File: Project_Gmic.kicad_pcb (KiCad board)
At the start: 2 copper layers, 55.9 x 62.2 mm, 50 parts, among them J1 USB4085-GF-A, J2 SJ1-3523N, SW1 SW_SPDT, U1 MCP6479, U2 MCP6476U, U3 MCP6476U, U4 XC6351A120MR-G

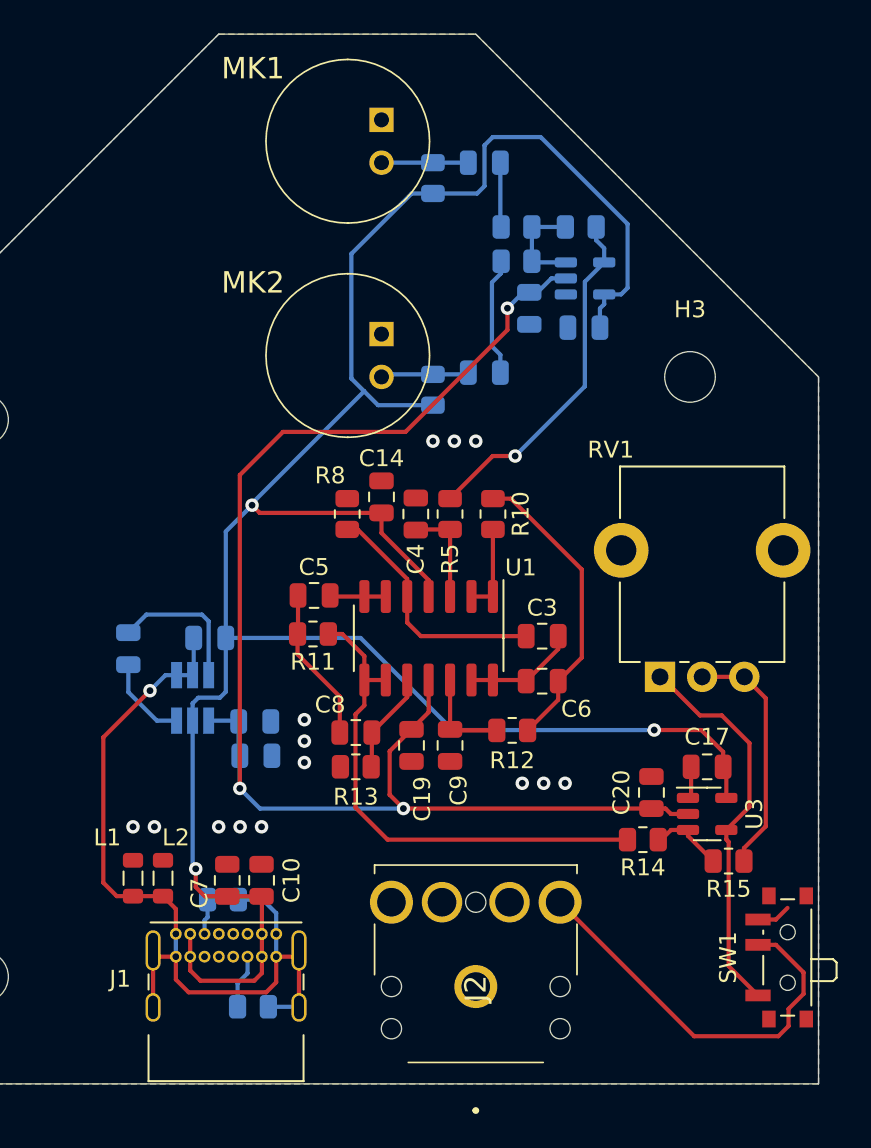
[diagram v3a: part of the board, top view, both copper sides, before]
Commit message: BOM, finishing PCB, changing some non-available components
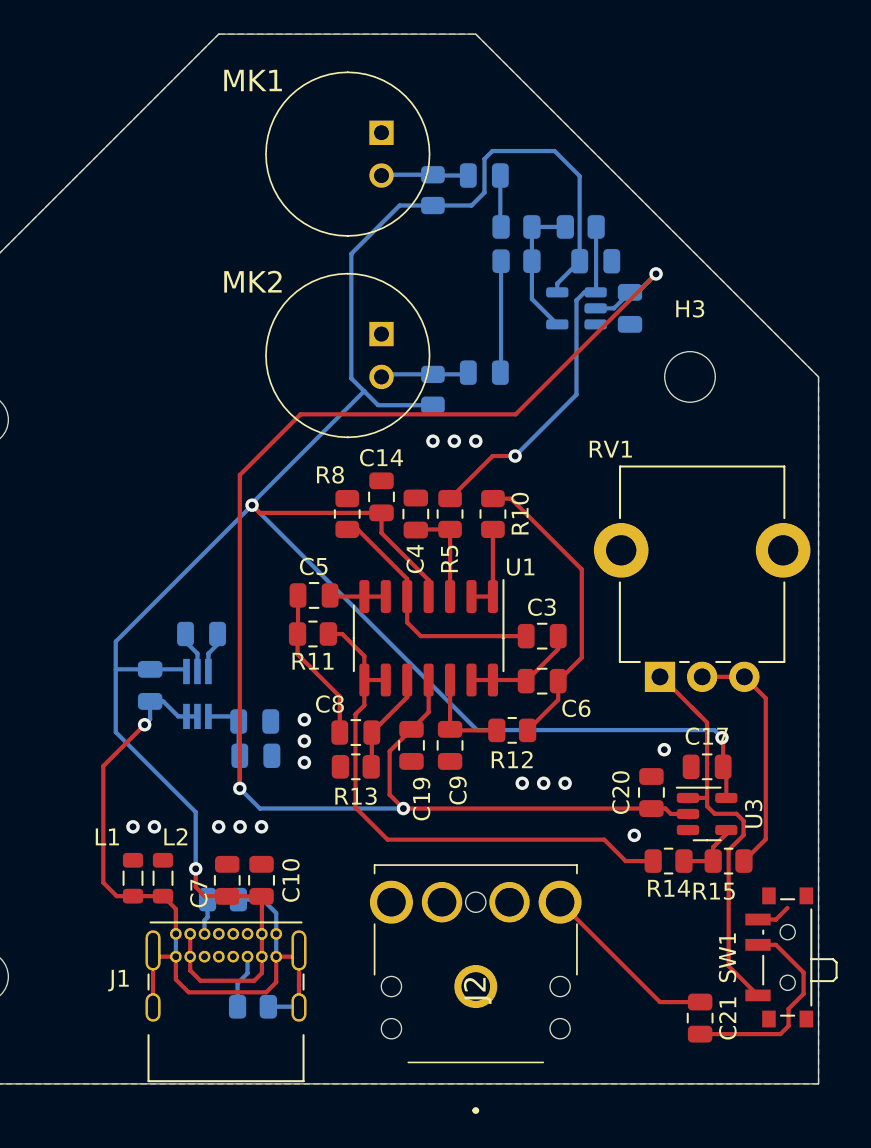
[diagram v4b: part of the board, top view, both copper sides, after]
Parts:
- added C21: NC, Capacitor_SMD:C_0805_2012Metric, F.Cu at (97.1, 149.8)
- R1, R2: value 2k2 -> 2.2k
- SW1: value SW_SPDT -> PCM12SMTR
- U2, U3: value MCP6476U -> AD8531
- U4: value XC6351A120MR-G -> MAX1852; footprint Package_TO_SOT_SMD:SOT-23-6_Handsoldering -> Package_TO_SOT_SMD:SOT-363_SC-70-6_Handsoldering
- moved C18 5.97 mm to (93.0, 107.7)
- moved C16 4.52 mm to (64.5, 130.0), turned to 270 degrees
- moved C15 4.43 mm to (67.6, 127.0), turned to 180 degrees
- moved C13 4.00 mm to (90.9, 104.9), turned to 0 degrees
- moved R14 1.98 mm to (95.2, 140.5)
- moved U2 1.85 mm to (89.8, 107.7), turned to 180 degrees
- moved C1 0.76 mm to (84.3, 99.8)
- moved MK1 0.76 mm to (78.2, 97.3)
- moved R1 0.72 mm to (81.3, 100.7)
- moved U4 0.37 mm to (67.3, 130.6), turned to 90 degrees
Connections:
- J2 pad 2: Net-(J2-Pad2) -> Net-(C21-Pad1)
- SW1 pad 2: Net-(J2-Pad2) -> Net-(C21-Pad2)
- U2 pad 1: GNDA -> /AUDIO_AVERAGE
- U2 pad 3: Net-(R6-Pad1) -> GNDA
- U2 pad 4: /AUDIO_AVERAGE -> Net-(R6-Pad1)
- U3 pad 1: GNDA -> /AUDIO_OUT
- U3 pad 3: Net-(R14-Pad1) -> GNDA
- U3 pad 4: /AUDIO_OUT -> Net-(R14-Pad1)
- U4 pad 1: GND -> -5V
- U4 pad 3: Net-(C15-Pad1) -> GND
- U4 pad 4: -5V -> +5V
- U4 pad 5: +5V -> Net-(C15-Pad2)
- U4 pad 6: Net-(C15-Pad2) -> Net-(C15-Pad1)
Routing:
- net Net-(J2-Pad2): track 24.0 -> 0.00 mm
- net Net-(C21-Pad2): track 0.00 -> 12.4 mm
- net Net-(C21-Pad1): track 0.00 -> 11.5 mm
- net -5V: track 85.4 -> 95.0 mm
- net Net-(C15-Pad1): track 8.56 -> 2.45 mm
- net +5V: track 142.1 -> 146.9 mm
- net Net-(C15-Pad2): track 5.19 -> 2.52 mm
- net GND: track 51.6 -> 49.0 mm
- net Net-(R6-Pad1): track 6.06 -> 8.48 mm
- net /AUDIO_PASS_HIGH: track 30.1 -> 32.1 mm
- net GNDA: track 3.96 -> 2.04 mm, vias 14 -> 16
- net /AUDIO_OUT: track 23.2 -> 24.7 mm
- net /AUDIO_1_IN: track 3.83 -> 3.07 mm
- net /AUDIO_AVERAGE: track 20.9 -> 21.5 mm
- net Net-(R14-Pad1): track 4.46 -> 3.90 mm

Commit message: Finalizing PCB, gerbert file
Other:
- rule pad_to_mask_clearance: 0.051 -> 0
- board text added: "GG"
- board text added: "GMIC V1.0"
- board text added: "Licensed under CERN-OHL-W v2 or later"

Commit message: moving to kicad 7, redo simulations WIP
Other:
- net class Default removed

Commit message: updating schematic, updating BOM
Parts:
- removed L1, L2: BLM21PG331SN1D, Inductor_SMD:L_0805_2012Metric
- added C22: 1uF, Capacitor_SMD:C_0805_2012Metric, F.Cu at (127.8, 130.5)
- added C23: 1uF, Capacitor_SMD:C_0805_2012Metric, F.Cu at (127.8, 133.5)
- added C24: 100nF, Capacitor_SMD:C_0805_2012Metric, F.Cu at (127.8, 136.5)
- added R16: 10k, Resistor_SMD:R_0805_2012Metric, F.Cu at (132.2, 134.9)
- added U5: TC1055, Package_TO_SOT_SMD:SOT-23-5, F.Cu at (132.6, 131.2)
- C10, C16: value 1uF -> 100nF
- C11, C17, C19: value 100nF -> 1uF
- C12: value 1uF -> 2.2uF
- C13, C20: value 100nF -> 2.2uF
- C21: value NC -> 100nF
- C8: value 100nF -> 100pF
- C9: value 100pF -> 1uF
- R10, R11, R8: value 80k -> 100k
- R14: value 100k -> 50k
- R15: value 80k -> 10k
- R2: value 2.2k -> 5.1k
- R3: value 5.1k -> 2.2k
- R6, R7: value 2.2k -> 80k
- RV1: value PTV09A-5025F-A503 -> PTV09A-4020F-A504; footprint Potentiometer_THT:Potentiometer_Alpha_RD901F-40-00D_Single_Vertical_CircularHoles -> PTV09A-4:PTV09A-4
- U1: value MCP6479 -> AD8532; footprint Package_SO:SOIC-14_3.9x8.7mm_P1.27mm -> Package_SO:SOIC-8_3.9x4.9mm_P1.27mm
- U2, U3: value AD8531 -> AD8532; footprint Package_TO_SOT_SMD:SOT-23-5 -> Package_SO:SOIC-8_3.9x4.9mm_P1.27mm
- U4: value MAX1852 -> AD8531; footprint Package_TO_SOT_SMD:SOT-363_SC-70-6_Handsoldering -> Package_TO_SOT_SMD:SOT-23-5
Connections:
- C10 pad 1: +5V -> +3.3V
- C11 pad 1: GNDA -> +3.3V
- C11 pad 2: -5V -> GNDA
- C12 pad 1: GNDA -> /AUDIO_OUT
- C12 pad 2: -5V -> /AUDIO_PASS_HIGH
- C13 pad 1: +5V -> Net-(U4-+)
- C14 pad 1: +5V -> +3.3V
- C15 pad 1: Net-(C15-Pad1) -> +3.3V
- C15 pad 2: Net-(C15-Pad2) -> GNDA
- C16 pad 1: +5V -> +3.3V
- C16 pad 2: GND -> GNDA
- C17 pad 1: +5V -> +3.3V
- C18 pad 1: GNDA -> +5V
- C18 pad 2: -5V -> GNDA
- C19 pad 1: GNDA -> +5V
- C19 pad 2: -5V -> GNDA
- C2 pad 2: Net-(C2-Pad2) -> Net-(MK2-+)
- C20 pad 1: GNDA -> +5V
- C20 pad 2: -5V -> GNDA
- C21 pad 1: Net-(C21-Pad1) -> +5V
- C21 pad 2: Net-(C21-Pad2) -> GNDA
- C4 pad 2: Net-(C4-Pad2) -> Net-(U2B-+)
- C5 pad 1: Net-(C5-Pad1) -> Net-(U3B-+)
- C5 pad 2: Net-(C5-Pad2) -> Net-(C3-Pad1)
- C7 pad 1: +5V -> +3.3V
- C8 pad 1: Net-(C8-Pad1) -> GNDA
- C8 pad 2: Net-(C5-Pad1) -> Net-(U3A-+)
- C9 pad 1: GNDA -> +3.3V
- C9 pad 2: Net-(C9-Pad2) -> GNDA
- J1 pad A1: GND -> GNDA
- J1 pad A12: GND -> GNDA
- J1 pad A6: Net-(J1-PadA6) -> unconnected-(J1-D+-PadA6)
- J1 pad A7: Net-(J1-PadA7) -> unconnected-(J1-D--PadA7)
- J1 pad A8: Net-(J1-PadA8) -> unconnected-(J1-SBU1-PadA8)
- J1 pad B1: GND -> GNDA
- J1 pad B12: GND -> GNDA
- J1 pad B5: Net-(J1-PadB5) -> Net-(J1-CC2)
- J1 pad B6: Net-(J1-PadB6) -> unconnected-(J1-D+-PadB6)
- J1 pad B7: Net-(J1-PadB7) -> unconnected-(J1-D--PadB7)
- J1 pad B8: Net-(J1-PadB8) -> unconnected-(J1-SBU2-PadB8)
- J1 pad S1: GND -> GNDA
- J2 pad 10: Net-(J2-Pad10) -> unconnected-(J2-Pad10)
- J2 pad 11: Net-(J2-Pad11) -> unconnected-(J2-Pad11)
- J2 pad 2: Net-(C21-Pad1) -> Net-(SW1-B)
- J2 pad 3: Net-(J2-Pad3) -> Net-(SW1-B)
- MK2 pad 2: Net-(C2-Pad2) -> Net-(MK2-+)
- R1 pad 1: +5V -> +3.3V
- R10 pad 1: Net-(C6-Pad2) -> Net-(U2A--)
- R11 pad 1: /AUDIO_PASS_HIGH -> Net-(U2A--)
- R11 pad 2: Net-(C5-Pad1) -> Net-(R11-Pad2)
- R12 pad 1: Net-(C9-Pad2) -> Net-(C6-Pad2)
- R12 pad 2: Net-(C6-Pad2) -> Net-(U2B--)
- R13 pad 1: GNDA -> Net-(U3A-+)
- R13 pad 2: Net-(C8-Pad1) -> Net-(C6-Pad2)
- R14 pad 1: Net-(R14-Pad1) -> /AUDIO_AVERAGE
- R14 pad 2: /AUDIO_PASS_HIGH -> Net-(R14-Pad2)
- R15 pad 1: Net-(R15-Pad1) -> +3.3V
- R15 pad 2: Net-(R14-Pad1) -> Net-(U4-+)
- R2 pad 1: +5V -> Net-(J1-CC2)
- R2 pad 2: Net-(C2-Pad2) -> GNDA
- R3 pad 1: Net-(J1-PadB5) -> +3.3V
- R3 pad 2: GND -> Net-(MK2-+)
- R4 pad 2: GND -> GNDA
- R5 pad 1: Net-(C4-Pad2) -> Net-(U2B-+)
- R6 pad 1: Net-(R6-Pad1) -> /AUDIO_PASS_HIGH
- R6 pad 2: /AUDIO_1_IN -> Net-(C3-Pad1)
- R7 pad 1: Net-(R6-Pad1) -> /V_OFFSET
- R7 pad 2: /AUDIO_2_IN -> Net-(U3B-+)
- R8 pad 1: GNDA -> Net-(R10-Pad2)
- R8 pad 2: Net-(C3-Pad1) -> /AUDIO_1_IN
- R9 pad 1: /AUDIO_AVERAGE -> Net-(R11-Pad2)
- R9 pad 2: Net-(R6-Pad1) -> /AUDIO_2_IN
- RV1 pad 1: /AUDIO_OUT -> unconnected-(RV1-Pad1)
- RV1 pad 2: Net-(R15-Pad1) -> Net-(U2A--)
- RV1 pad 3: Net-(R15-Pad1) -> Net-(R14-Pad2)
- SW1 pad 2: Net-(C21-Pad2) -> Net-(SW1-B)
- U1 pad 2: Net-(R10-Pad2) -> /AUDIO_1_IN
- U1 pad 3: Net-(C4-Pad2) -> /V_OFFSET
- U1 pad 4: +5V -> GNDA
- U1 pad 5: Net-(C3-Pad1) -> /V_OFFSET
- U1 pad 6: Net-(C5-Pad2) -> /AUDIO_2_IN
- U1 pad 7: Net-(C5-Pad2) -> Net-(R11-Pad2)
- U1 pad 8: /AUDIO_PASS_HIGH -> +3.3V
- U2 pad 2: -5V -> Net-(U2A--)
- U2 pad 3: GNDA -> /V_OFFSET
- U2 pad 4: Net-(R6-Pad1) -> GNDA
- U2 pad 5: +5V -> Net-(U2B-+)
- U3 pad 1: /AUDIO_OUT -> /AUDIO_PASS_LOW
- U3 pad 2: -5V -> /AUDIO_PASS_LOW
- U3 pad 3: GNDA -> Net-(U3A-+)
- U3 pad 4: Net-(R14-Pad1) -> GNDA
- U3 pad 5: +5V -> Net-(U3B-+)
- U4 pad 1: -5V -> /V_OFFSET
- U4 pad 2: GND -> GNDA
- U4 pad 3: GND -> Net-(U4-+)
- U4 pad 4: +5V -> /V_OFFSET
- U4 pad 5: Net-(C15-Pad2) -> +3.3V
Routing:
- net +5V: track 146.9 -> 0.00 mm, vias 3 -> 0
- net -5V: track 95.0 -> 0.00 mm, vias 3 -> 0
- net GND: track 49.0 -> 0.00 mm, vias 1 -> 0
- net /AUDIO_PASS_HIGH: track 32.1 -> 0.00 mm
- net /AUDIO_OUT: track 24.7 -> 0.00 mm
- net /AUDIO_AVERAGE: track 21.5 -> 0.00 mm, vias 1 -> 0
- net Net-(C6-Pad2): track 17.9 -> 0.00 mm
- net Net-(C3-Pad1): track 14.7 -> 0.00 mm
- net Net-(R15-Pad1): track 14.5 -> 0.00 mm
- net Net-(C21-Pad2): track 12.4 -> 0.00 mm
- net Net-(C21-Pad1): track 11.5 -> 0.00 mm
- net Net-(C5-Pad1): track 9.18 -> 0.00 mm
- net Net-(R6-Pad1): track 8.48 -> 0.00 mm
- net /AUDIO_PASS_LOW: track 6.72 -> 0.00 mm
- net /AUDIO_2_IN: track 6.62 -> 0.00 mm
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
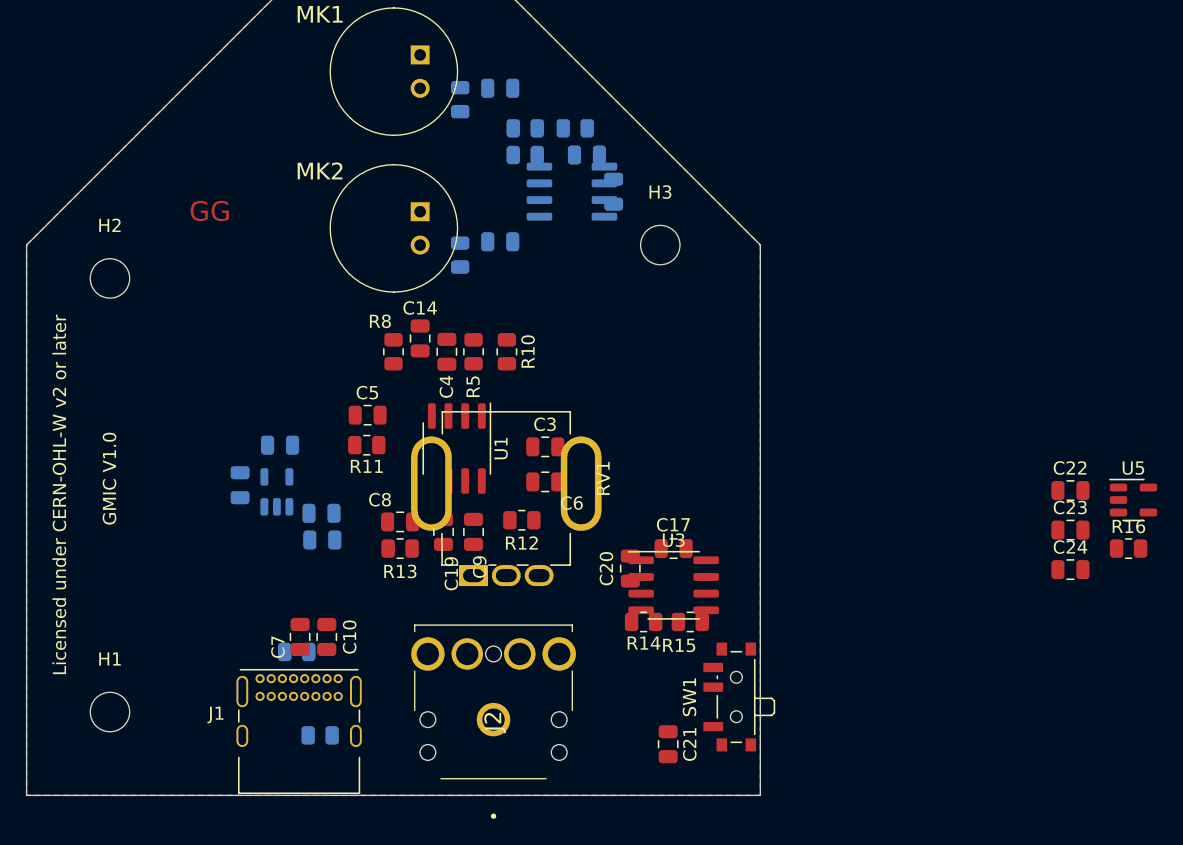
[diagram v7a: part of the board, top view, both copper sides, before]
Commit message: update PCB, finish placement and first routing
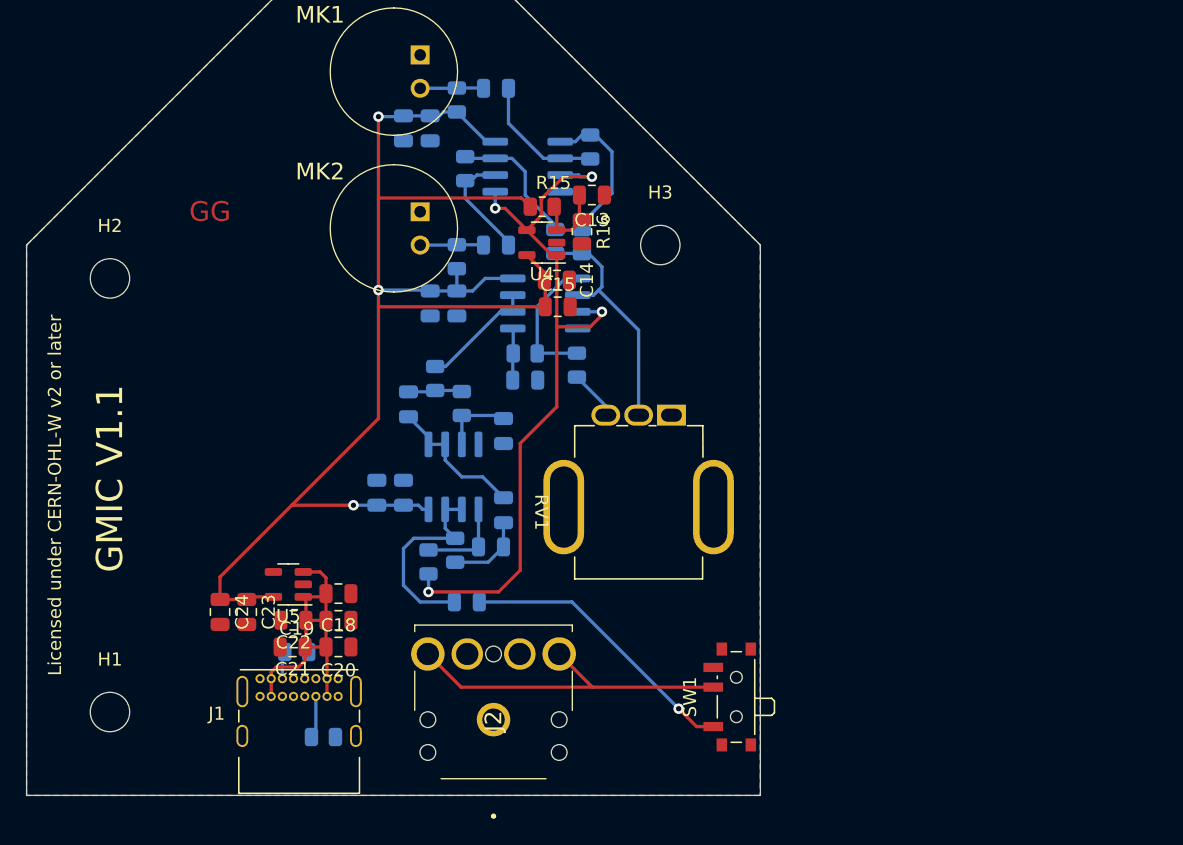
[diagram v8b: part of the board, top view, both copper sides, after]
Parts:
- C10, C17, C3, C4, C5, C6, C7, C8, C9, R10, R11, R12, R13, R14, R5, R8, U1, U3: moved to B.Cu
- C13, C15, C18, U4: moved to F.Cu
- moved C24 64.8 mm to (63.0, 139.7), turned to -90 degrees
- moved U5 64.7 mm to (68.2, 137.6), turned to 180 degrees
- moved C23 63.0 mm to (65.0, 139.7), turned to -90 degrees
- moved C22 60.0 mm to (68.6, 140.3), turned to 180 degrees
- moved R16 48.1 mm to (90.6, 110.7), turned to -90 degrees
- moved C7 40.0 mm to (79.0, 102.9), turned to -90 degrees
- moved R2 38.2 mm to (70.9, 149.2), turned to 0 degrees
- moved R3 37.9 mm to (81.0, 112.6), turned to 90 degrees
- moved C18 37.1 mm to (72.0, 138.3), turned to 0 degrees
- moved R15 33.6 mm to (87.5, 108.8), turned to 0 degrees
- moved R6 32.6 mm to (80.9, 135.0), turned to -90 degrees
- moved R7 31.9 mm to (78.9, 135.9), turned to 90 degrees
- moved C9 31.2 mm to (77.0, 102.9), turned to -90 degrees
- moved C21 29.5 mm to (68.5, 142.4), turned to 180 degrees
- moved U4 27.7 mm to (87.5, 111.6), turned to 180 degrees
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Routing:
- net +3.3V: track 0.00 -> 107.8 mm, vias 0 -> 3
- net /V_OFFSET: track 0.00 -> 57.4 mm, vias 0 -> 4
- net Net-(SW1-B): track 0.00 -> 26.4 mm
- net +5V: track 0.00 -> 25.7 mm
- net /AUDIO_OUT: track 0.00 -> 21.7 mm, vias 0 -> 1
- net Net-(U2A--): track 0.00 -> 18.4 mm
- net /AUDIO_PASS_HIGH: track 0.00 -> 15.2 mm
- net Net-(R10-Pad2): track 0.00 -> 11.6 mm
- net /AUDIO_PASS_LOW: track 0.00 -> 10.8 mm
- net /AUDIO_AVERAGE: track 0.00 -> 10.6 mm
- net Net-(R11-Pad2): track 0.00 -> 10.4 mm
- net /AUDIO_1_IN: track 0.00 -> 10.0 mm
- net Net-(U2B--): track 0.00 -> 8.90 mm
- net /AUDIO_2_IN: track 0.00 -> 8.74 mm
- net Net-(U3B-+): track 0.00 -> 6.76 mm
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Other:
- board text added: "GMIC V1.1"
- board text removed: "GMIC V1.0"
